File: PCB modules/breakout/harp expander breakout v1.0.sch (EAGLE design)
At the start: 13 parts, among them SW1 693-1301.9302, SW2 693-1301.9302

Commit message: Corrected silkscreen and minor change to top layer.
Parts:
- removed SW2: 693-1301.9302, SparkFun-Electromechanical:TAC_SWITCHPTH
- added SW0: 693-1301.9302, SparkFun-Electromechanical:TAC_SWITCHPTH
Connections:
- net GND: now also SW0.4; no longer SW2.4
- net N$14: now also SW1.2; no longer SW2.2
- net N$24: now also SW0.2; no longer SW1.2
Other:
- moved on the sheet: SW1

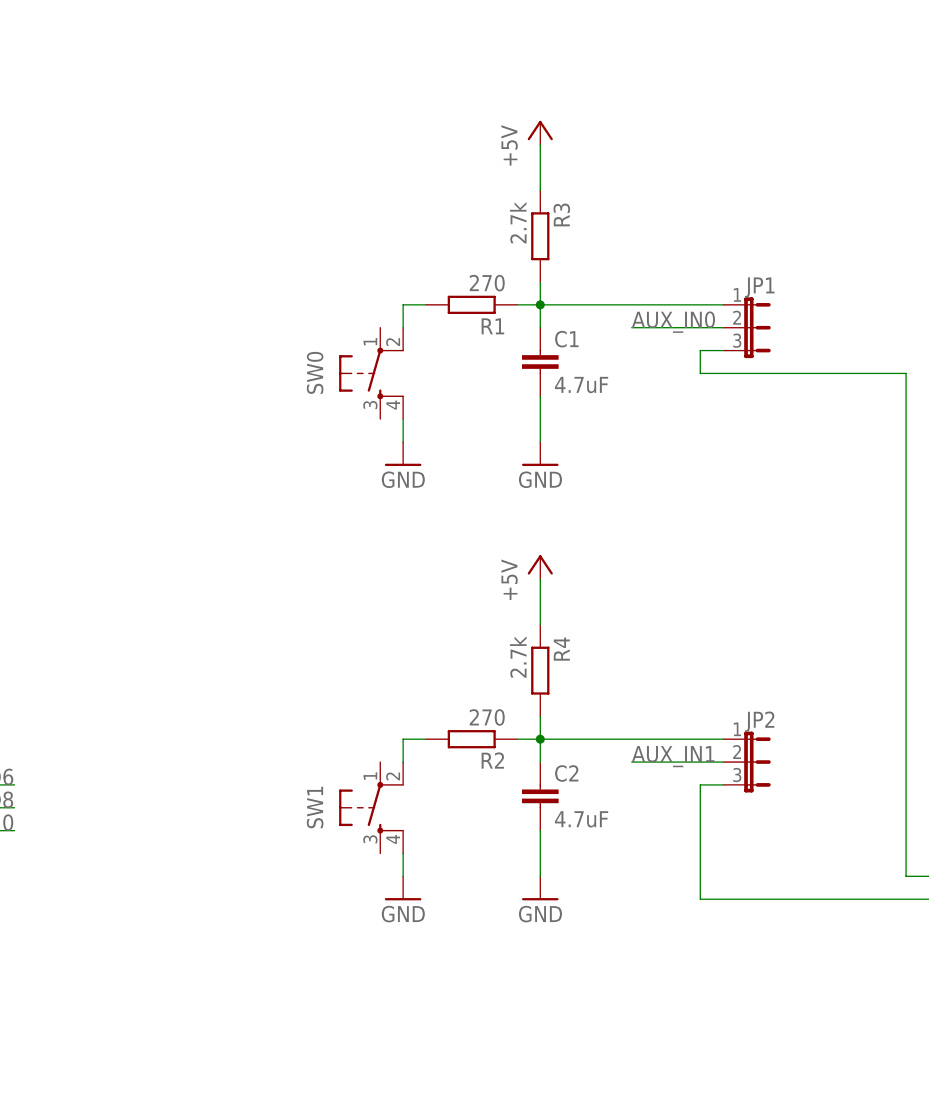
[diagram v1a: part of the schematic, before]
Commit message: Corrected wrong buttons polarity.
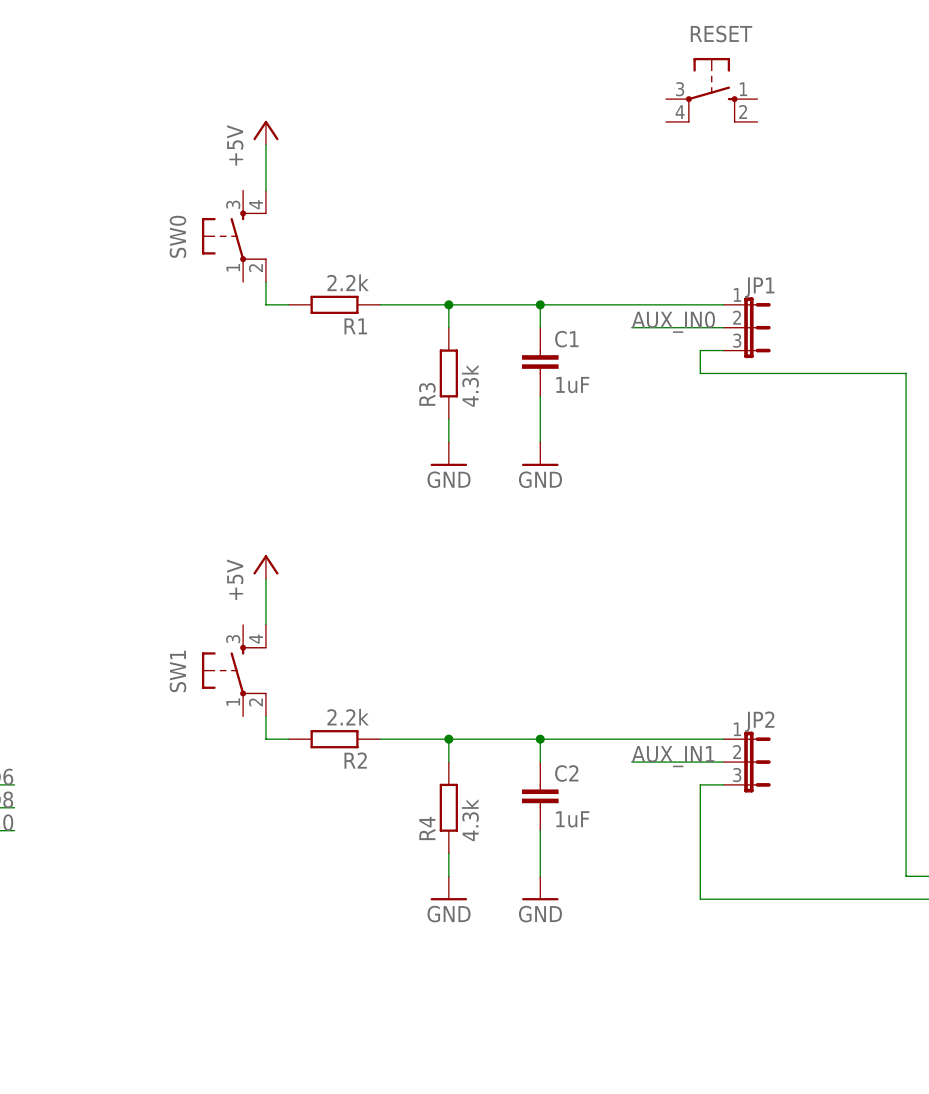
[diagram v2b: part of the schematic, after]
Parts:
- added RESET: (no value), switch-omron:40-XX
- C1, C2: value 4.7uF -> 1uF
- R1, R2: value 270 -> 2.2k
- R3, R4: value 2.7k -> 4.3k
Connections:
- net +5V: now also SW0.4, SW1.4; no longer R3.1, R4.1
- net GND: now also R3.1, R4.1; no longer SW0.4, SW1.4
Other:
- moved on the sheet: R1, R2, R3, R4, SW0, SW1

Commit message: Updated files for final revision before production.
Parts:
- removed RESET: (no value), switch-omron:40-XX
- SW0: value 693-1301.9302 -> (none); device SparkFun-Electromechanical:TAC_SWITCHPTH -> switch-omron:40-XX; MF (none) -> OMRON COMPONENTS USA; MPN (none) -> B3F-4000; OC_FARNELL (none) -> 176434; OC_NEWARK (none) -> 36K3105
- SW1: value 693-1301.9302 -> (none); device SparkFun-Electromechanical:TAC_SWITCHPTH -> switch-omron:40-XX
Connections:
- net +5V: now also SW0.P1, SW1.P1; no longer SW0.4, SW1.4
- net N$14: now also SW1.S1; no longer SW1.2
- net N$24: now also SW0.S1; no longer SW0.2
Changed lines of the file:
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@@
 <part name="GND22" library="supply1" deviceset="GND" device=""/>
 <part name="GND31" library="supply1" deviceset="GND" device=""/>
-<part name="SW1" library="SparkFun-Electromechanical" deviceset="TAC_SWITCH" device="PTH" value="693-1301.9302"/>
 <part name="R2" library="rcl" deviceset="R-EU_" device="R0603" value="2.2k"/>
 <part name="R4" library="rcl" deviceset="R-EU_" device="R0603" value="4.3k"/>
 <part name="C2" library="rcl" deviceset="C-EU" device="C0603" value="1uF"/>
 <part name="GND32" library="supply1" deviceset="GND" device=""/>
-<part name="SW0" library="SparkFun-Electromechanical" deviceset="TAC_SWITCH" device="PTH" value="693-1301.9302"/>
 <part name="R1" library="rcl" deviceset="R-EU_" device="R0603" value="2.2k"/>
 <part name="R3" library="rcl" deviceset="R-EU_" device="R0603" value="4.3k"/>
@@
 <part name="P+2" library="supply1" deviceset="+5V" device="" value="+5V"/>
 <part name="GND2" library="supply1" deviceset="GND" device=""/>
-<part name="RESET" library="switch-omron" deviceset="40-XX" device="">
+<part name="SW0" library="switch-omron" deviceset="40-XX" device="">
 <attribute name="MF" value="OMRON COMPONENTS USA"/>
 <attribute name="MPN" value="B3F-4000"/>
@@
 <attribute name="OC_NEWARK" value="36K3105"/>
 </part>
+<part name="SW1" library="switch-omron" deviceset="40-XX" device=""/>
 </parts>
 <sheets>
@@
 <attribute name="VALUE" x="198.12" y="78.74" size="1.778" layer="96" rot="MR0"/>
 </instance>
-<instance part="SW1" gate="S" x="116.84" y="93.98" smashed="yes" rot="R90">
-<attribute name="NAME" x="110.49" y="91.44" size="1.778" layer="95" rot="R90"/>
-</instance>
 <instance part="R2" gate="G$1" x="127" y="86.36" smashed="yes" rot="R180">
 <attribute name="NAME" x="130.81" y="84.8614" size="1.778" layer="95" rot="R180"/>
@@
 <attribute name="VALUE" x="152.4" y="66.04" size="1.778" layer="96" rot="MR0"/>
 </instance>
-<instance part="SW0" gate="S" x="116.84" y="142.24" smashed="yes" rot="R90">
-<attribute name="NAME" x="110.49" y="139.7" size="1.778" layer="95" rot="R90"/>
-</instance>
 <instance part="R1" gate="G$1" x="127" y="134.62" smashed="yes" rot="R180">
 <attribute name="NAME" x="130.81" y="133.1214" size="1.778" layer="95" rot="R180"/>
@@
 <attribute name="VALUE" x="142.24" y="66.04" size="1.778" layer="96" rot="MR0"/>
 </instance>
-<instance part="RESET" gate="1" x="168.91" y="157.48" smashed="yes" rot="R270">
-<attribute name="NAME" x="166.37" y="163.83" size="1.778" layer="95"/>
-<attribute name="VALUE" x="172.085" y="161.29" size="1.778" layer="96"/>
+<instance part="SW0" gate="1" x="116.84" y="142.24" smashed="yes" rot="MR180">
+<attribute name="NAME" x="110.49" y="144.78" size="1.778" layer="95" rot="MR270"/>
+<attribute name="VALUE" x="113.03" y="139.065" size="1.778" layer="96" rot="MR270"/>
+</instance>
+<instance part="SW1" gate="1" x="116.84" y="93.98" smashed="yes" rot="MR180">
+<attribute name="NAME" x="110.49" y="96.52" size="1.778" layer="95" rot="MR270"/>
+<attribute name="VALUE" x="113.03" y="90.805" size="1.778" layer="96" rot="MR270"/>
 </instance>
 </instances>
@@
 </segment>
 <segment>
-<pinref part="SW0" gate="S" pin="4"/>
+<pinref part="SW0" gate="1" pin="P1"/>
+<pinref part="P+1" gate="1" pin="+5V"/>
 <wire x1="119.38" y1="147.32" x2="119.38" y2="152.4" width="0.1524" layer="91"/>
-<pinref part="P+1" gate="1" pin="+5V"/>
-</segment>
-<segment>
-<pinref part="SW1" gate="S" pin="4"/>
-<wire x1="119.38" y1="99.06" x2="119.38" y2="104.14" width="0.1524" layer="91"/>
+</segment>
+<segment>
 <pinref part="P+2" gate="1" pin="+5V"/>
+<pinref part="SW1" gate="1" pin="P1"/>
+<wire x1="119.38" y1="104.14" x2="119.38" y2="99.06" width="0.1524" layer="91"/>
 </segment>
 </net>
@@
 <net name="N$14" class="0">
 <segment>
-<pinref part="SW1" gate="S" pin="2"/>
 <pinref part="R2" gate="G$1" pin="2"/>
-<wire x1="119.38" y1="88.9" x2="119.38" y2="86.36" width="0.1524" layer="91"/>
 <wire x1="119.38" y1="86.36" x2="121.92" y2="86.36" width="0.1524" layer="91"/>
+<pinref part="SW1" gate="1" pin="S1"/>
+<wire x1="119.38" y1="86.36" x2="119.38" y2="88.9" width="0.1524" layer="91"/>
 </segment>
 </net>
@@
 <net name="N$24" class="0">
 <segment>
-<pinref part="SW0" gate="S" pin="2"/>
 <pinref part="R1" gate="G$1" pin="2"/>
-<wire x1="119.38" y1="137.16" x2="119.38" y2="134.62" width="0.1524" layer="91"/>
 <wire x1="119.38" y1="134.62" x2="121.92" y2="134.62" width="0.1524" layer="91"/>
-</segment>
-</net>
+<pinref part="SW0" gate="1" pin="S1"/>
+<wire x1="119.38" y1="134.62" x2="119.38" y2="137.16" width="0.1524" layer="91"/>
+</segment>
+</net>
